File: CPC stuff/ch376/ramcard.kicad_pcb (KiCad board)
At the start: 2 copper layers, 69.1 x 40.4 mm, 17 parts, among them IC1 74LS20, IC2 74LS02, IC3 74LS138, IC4 CH376, P1 CONN_25X2, P2 USB_A, U1 LD1117S33CTR, U2 CONN_SD, Y1 Crystal_Small

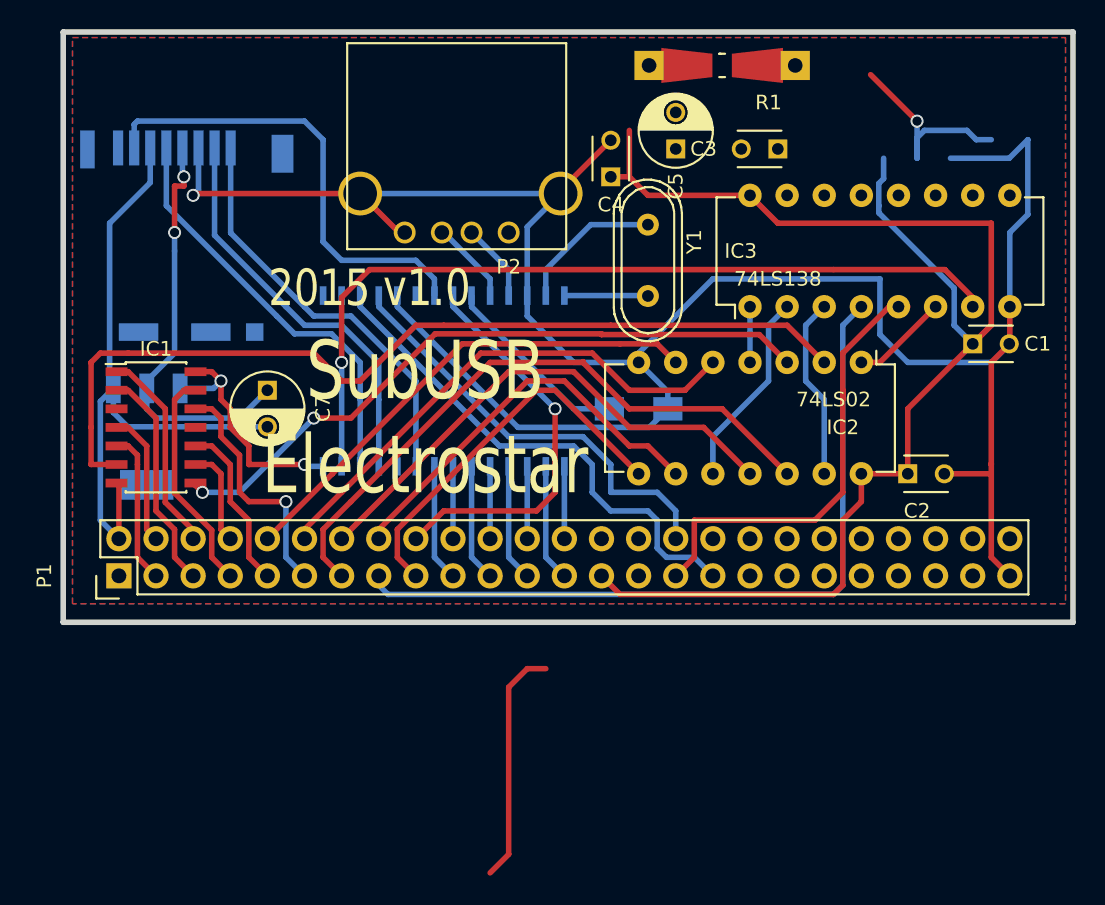
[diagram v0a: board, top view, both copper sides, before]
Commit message: Complete routing of Albireo, including serial port.
git-svn-id: svn://pulkomandy.tk/avrstuff@117 c6672c3c-f6b6-47f9-9001-1fd6b12fecbe
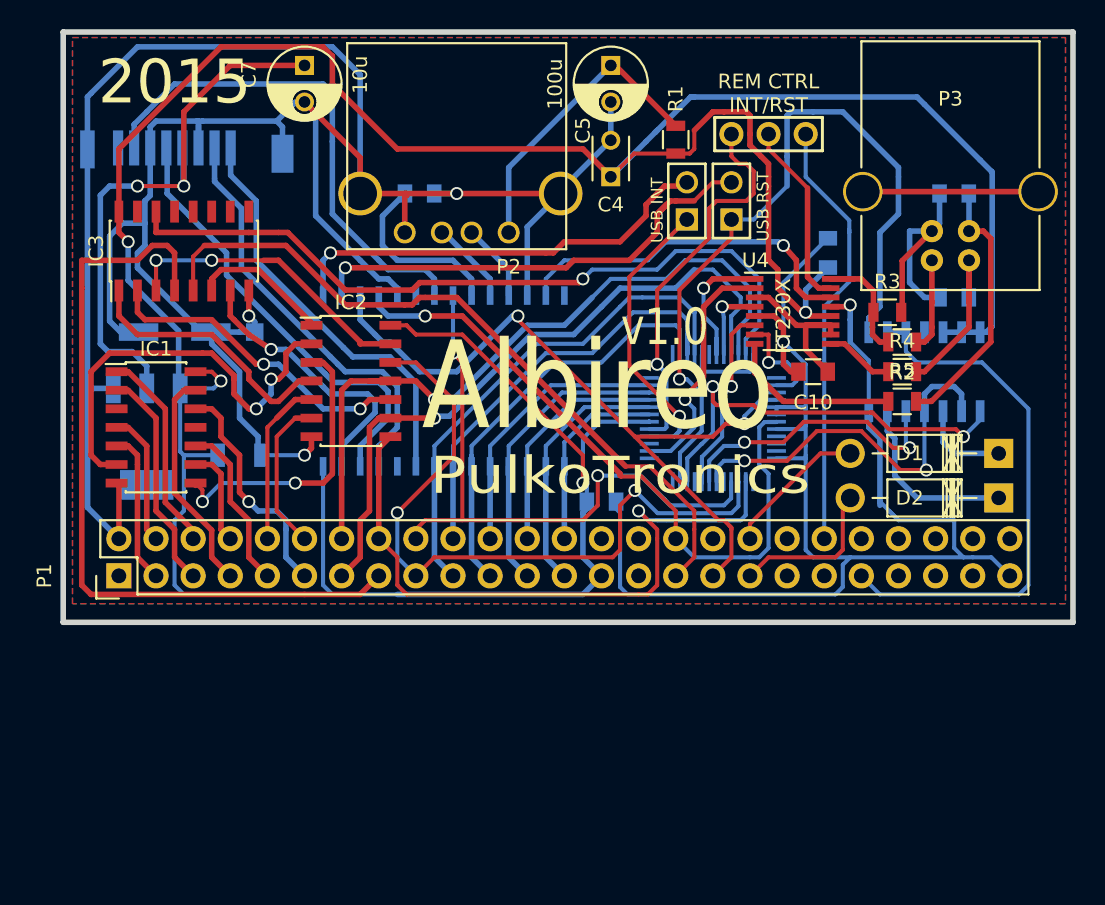
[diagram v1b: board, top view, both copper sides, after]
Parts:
- removed Y1: Crystal_Small, Crystals:Crystal_HC49-U_Vertical
- added C10: C, Capacitors_SMD:C_0805, F.Cu at (69.1, 53.3)
- added C8: 47pF, Capacitors_SMD:C_0805, B.Cu at (78.7, 41.1)
- added C9: 47pF, Capacitors_SMD:C_0805, B.Cu at (78.7, 48.3)
- added D1: D, Diodes_ThroughHole:Diode_DO-41_SOD81_Horizontal_RM10, F.Cu at (81.8, 58.9)
- added D2: D, Diodes_ThroughHole:Diode_DO-41_SOD81_Horizontal_RM10, F.Cu at (81.8, 62.0)
- added JP1: JUMPER3, opendous:SIL-3-Blank, F.Cu at (66.0, 37.1)
- added JP2: USB INT, opendous:SIL-2_Opendous, F.Cu at (60.5, 41.7)
- added JP3: USB RST, opendous:SIL-2_Opendous, F.Cu at (63.5, 41.7)
- added P3: USB_B, Connect:USB_B, F.Cu at (77.2, 45.7)
- added R2: 4k7, Resistors_SMD:R_0805, F.Cu at (75.2, 51.3)
- added R3: 10k, Resistors_SMD:R_0805, F.Cu at (74.2, 49.3)
- added R4: 27, Resistors_SMD:R_0805, F.Cu at (75.2, 53.3)
- added R5: 27, Resistors_SMD:R_0805, F.Cu at (75.2, 55.4)
- added U3: TL16C550C, Housings_QFP:TQFP-48_7x7mm_Pitch0.5mm, B.Cu at (62.2, 56.5)
- added U4: FT230X, Housings_SSOP:SSOP-16_3.9x4.9mm_Pitch0.635mm, F.Cu at (67.7, 49.2)
- added U5: 74LS00, Housings_SOIC:SOIC-14_3.9x8.7mm_Pitch1.27mm, B.Cu at (76.7, 53.3)
- C1, C2: footprint Capacitors_ThroughHole:C_Disc_D3_P2.5 -> Capacitors_SMD:C_0805; moved to B.Cu
- C3: footprint Capacitors_ThroughHole:C_Disc_D3_P2.5 -> Capacitors_SMD:C_1206; moved to B.Cu
- C6: footprint Capacitors_SMD:C_1206_HandSoldering -> Capacitors_SMD:C_0805
- IC2: footprint Housings_DIP:DIP-14_W7.62mm -> Housings_SOIC:SOIC-14_3.9x8.7mm_Pitch1.27mm
- IC3: footprint Housings_DIP:DIP-16_W7.62mm -> Housings_SOIC:SOIC-16_3.9x9.9mm_Pitch1.27mm
- R1: footprint Resistors_Universal:Resistor_SMD+THTuniversal_0805to1206_RM10_HandSoldering -> Resistors_SMD:R_0805
- moved C3 42.4 mm to (29.8, 59.1), turned to 0 degrees
- moved IC3 38.9 mm to (26.0, 45.1)
- moved IC2 34.9 mm to (37.5, 54.0), turned to 0 degrees
- moved C7 22.4 mm to (34.3, 32.4)
- moved C2 21.0 mm to (54.6, 62.2)
- moved C6 21.0 mm to (42.2, 41.1)
- moved C1 11.7 mm to (70.1, 45.2), turned to 90 degrees
- moved C5 7.24 mm to (55.2, 32.4), turned to 270 degrees
- moved R1 5.99 mm to (59.7, 37.5), turned to 270 degrees
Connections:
- IC2 pad 12: /A5 -> /A1
- IC2 pad 5: /A6 -> /A8
- IC2 pad 6: /A8 -> /A6
- IC2 pad 8: /A1 -> /A2
- IC2 pad 9: /A2 -> /A5
- IC3 pad 14: (no net) -> /FEBx
- IC4 pad 1: (no net) -> Net-(IC4-Pad1)
- IC4 pad 13: Net-(IC4-Pad13) -> /12MHz
- IC4 pad 14: Net-(IC4-Pad14) -> (no net)
- IC4 pad 2: (no net) -> Net-(IC4-Pad2)
- P1 pad 35: (no net) -> //INT
- P1 pad 36: (no net) -> //NMI
- P1 pad 40: (no net) -> /BUSRST
- P1 pad 41: (no net) -> //RESET
- U2 pad 9: Net-(U2-Pad9) -> GND
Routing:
- net VCC: track 112.7 -> 274.5 mm, vias 2 -> 4
- net GND: track 203.6 -> 341.5 mm, vias 1 -> 5
- net /PRESET: track 0.00 -> 52.3 mm, vias 0 -> 1
- net /FEBx: track 0.00 -> 51.8 mm, vias 0 -> 1
- net /FE80: track 57.7 -> 19.3 mm
- net //RESET: track 0.00 -> 36.9 mm
- net Net-(IC4-Pad2): track 0.00 -> 32.5 mm, vias 0 -> 1
- net (no net): track 30.3 -> 0.00 mm, vias 1 -> 0
- net Net-(IC4-Pad1): track 0.00 -> 30.0 mm, vias 0 -> 1
- net /BUSRST: track 0.00 -> 29.6 mm
- net //OUT1: track 0.00 -> 28.6 mm, vias 0 -> 2
- net //RI: track 0.00 -> 26.9 mm, vias 0 -> 1
- net /INTRPT: track 0.00 -> 26.8 mm, vias 0 -> 2
- net /D7: track 8.02 -> 34.7 mm
- net Net-(IC1-Pad8): track 46.2 -> 20.0 mm
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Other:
- net class Default: clearance 0.2032 -> 0.2
- rule trace_clearance: 0.2032 -> 0.2
- board text added: "2015"
- board text added: "Albireo"
- board text added: "REM CTRL INT/RST"
- board text added: "v1.0"
- board text removed: "2015 v1.0"
- board text removed: "SubUSB Electrostar"

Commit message: Update following Gerald's coomments  * Use 74LS38 instead of 74LS00 and remove diodes  * Add pull-up for the one pin that doesn't have one (PRESET)  * Optimize layout a bit
git-svn-id: svn://pulkomandy.tk/avrstuff@118 c6672c3c-f6b6-47f9-9001-1fd6b12fecbe
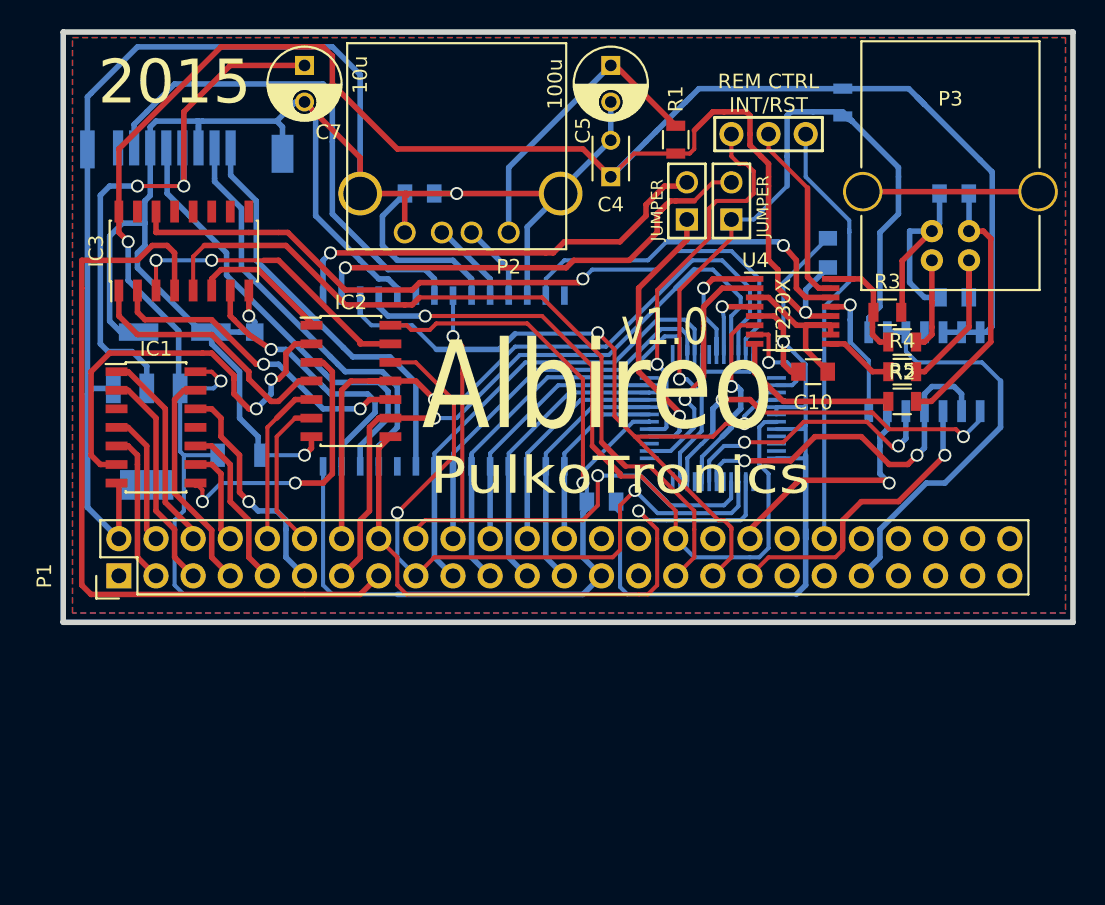
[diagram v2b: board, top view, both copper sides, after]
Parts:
- removed D1, D2: D, Diodes_ThroughHole:Diode_DO-41_SOD81_Horizontal_RM10
- added R6: 4K7, Resistors_SMD:R_0805, B.Cu at (71.1, 34.9)
- JP2: value USB INT -> JUMPER
- JP3: value USB RST -> JUMPER
- U5: value 74LS00 -> 74LS38
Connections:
- U5 pad 3: Net-(D1-Pad1) -> //INT
- U5 pad 6: Net-(D2-Pad1) -> //NMI
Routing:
- net GND: track 341.5 -> 314.1 mm
- net Net-(D2-Pad1): track 12.4 -> 0.00 mm
- net //INT: track 10.9 -> 21.0 mm, vias 0 -> 1
- net //RESET: track 36.9 -> 27.9 mm
- net //NMI: track 9.87 -> 17.3 mm, vias 0 -> 1
- net Net-(D1-Pad1): track 6.25 -> 0.00 mm
- net //IORQ: track 49.9 -> 53.3 mm
- net VCC: track 274.5 -> 277.8 mm
- net /D6: track 30.7 -> 27.5 mm
- net //RD: track 47.4 -> 50.6 mm
- net /D7: track 34.7 -> 32.5 mm
- net //OUT1: track 28.6 -> 26.5 mm
- net /INTRPT: track 26.8 -> 25.1 mm
- net /PRESET: track 52.3 -> 53.7 mm
- net /D5: track 30.6 -> 29.3 mm
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
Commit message: A lot of tweaking and small fixes.
git-svn-id: svn://pulkomandy.tk/avrstuff@119 c6672c3c-f6b6-47f9-9001-1fd6b12fecbe
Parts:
- removed JP1: JUMPER3, opendous:SIL-3-Blank
- removed JP2, JP3: JUMPER, opendous:SIL-2_Opendous
- added R7: 4k7, Resistors_SMD:R_0805, F.Cu at (72.9, 48.3)
- added S1: SW_DIP_x4, Buttons_Switches_ThroughHole:SW_DIP_x4_Slide, F.Cu at (67.3, 41.3)
- C3: footprint Capacitors_SMD:C_1206 -> Capacitors_SMD:C_0805
- R2, R3: moved to B.Cu
- U4: value FT230X -> FT231X; footprint Housings_SSOP:SSOP-16_3.9x4.9mm_Pitch0.635mm -> ch376:SSOP-24_3.9x8.7mm_Pitch0.635mm
- moved R6 13.1 mm to (74.3, 47.6), turned to 180 degrees
- moved R2 11.4 mm to (69.8, 41.3), turned to 270 degrees
- moved P3 9.65 mm to (72.0, 37.6), turned to 0 degrees
- moved C9 8.08 mm to (73.0, 42.5), turned to 0 degrees
- moved R1 7.24 mm to (55.2, 43.2), turned to 90 degrees
- moved R5 7.22 mm to (76.5, 48.3), turned to 90 degrees
- moved R4 5.11 mm to (74.7, 48.3), turned to 90 degrees
- moved R3 4.68 mm to (73.2, 44.7)
- moved C8 3.42 mm to (76.2, 38.9), turned to 90 degrees
- moved C1 3.23 mm to (67.8, 47.5), turned to 180 degrees
- moved C10 2.22 mm to (68.2, 55.4)
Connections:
- IC4 pad 1: Net-(IC4-Pad1) -> /INT
- IC4 pad 2: Net-(IC4-Pad2) -> /RSTI
- P1 pad 46: (no net) -> /CURSOR
- U3 pad 39: (no net) -> //DSR
- U3 pad 41: //RI -> /CURSOR
- U4 pad 1: /RX -> /GPO2
- U4 pad 10: Net-(C10-Pad1) -> /24MHz
- U4 pad 11: Net-(C10-Pad1) -> Net-(R5-Pad1)
- U4 pad 12: VCC -> Net-(R4-Pad1)
- U4 pad 13: GND -> Net-(C10-Pad1)
- U4 pad 14: /12MHz -> VCC
- U4 pad 15: /GPO2 -> VCC
- U4 pad 16: /VBUS_Sense -> GND
- U4 pad 5: GND -> (no net)
- U4 pad 6: //RTS -> GND
- U4 pad 7: /24MHz -> (no net)
- U4 pad 8: Net-(R5-Pad1) -> (no net)
- U4 pad 9: Net-(R4-Pad1) -> //RTS
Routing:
- net GND: track 314.1 -> 437.4 mm, vias 5 -> 6
- net /INT: track 0.00 -> 49.1 mm, vias 0 -> 2
- net /CURSOR: track 0.00 -> 37.4 mm, vias 0 -> 1
- net /RSTI: track 0.00 -> 35.2 mm, vias 0 -> 2
- net VCC: track 277.8 -> 244.7 mm
- net Net-(IC4-Pad2): track 32.5 -> 0.00 mm, vias 1 -> 0
- net Net-(IC4-Pad1): track 30.0 -> 0.00 mm, vias 1 -> 0
- net //RI: track 26.9 -> 0.00 mm, vias 1 -> 0
- net //DSR: track 0.00 -> 23.1 mm, vias 0 -> 1
- net Net-(P3-Pad5): track 12.0 -> 0.00 mm
- net +3V3: track 51.6 -> 40.1 mm
- net /A1: track 48.4 -> 59.8 mm
- net /GPO2: track 12.8 -> 23.6 mm
- net /A8: track 16.8 -> 27.1 mm
- net //DCD: track 19.7 -> 28.6 mm
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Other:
- board text added: "1 CH376 INT enable 2 CH376 Reset enable 3 Rem.ctrl resets CPC 4 Rem.ctrl triggers interrupt"
- board text added: "uSD"
- board text added: "v0.9"
- board text removed: "REM CTRL INT/RST"
- board text removed: "v1.0"

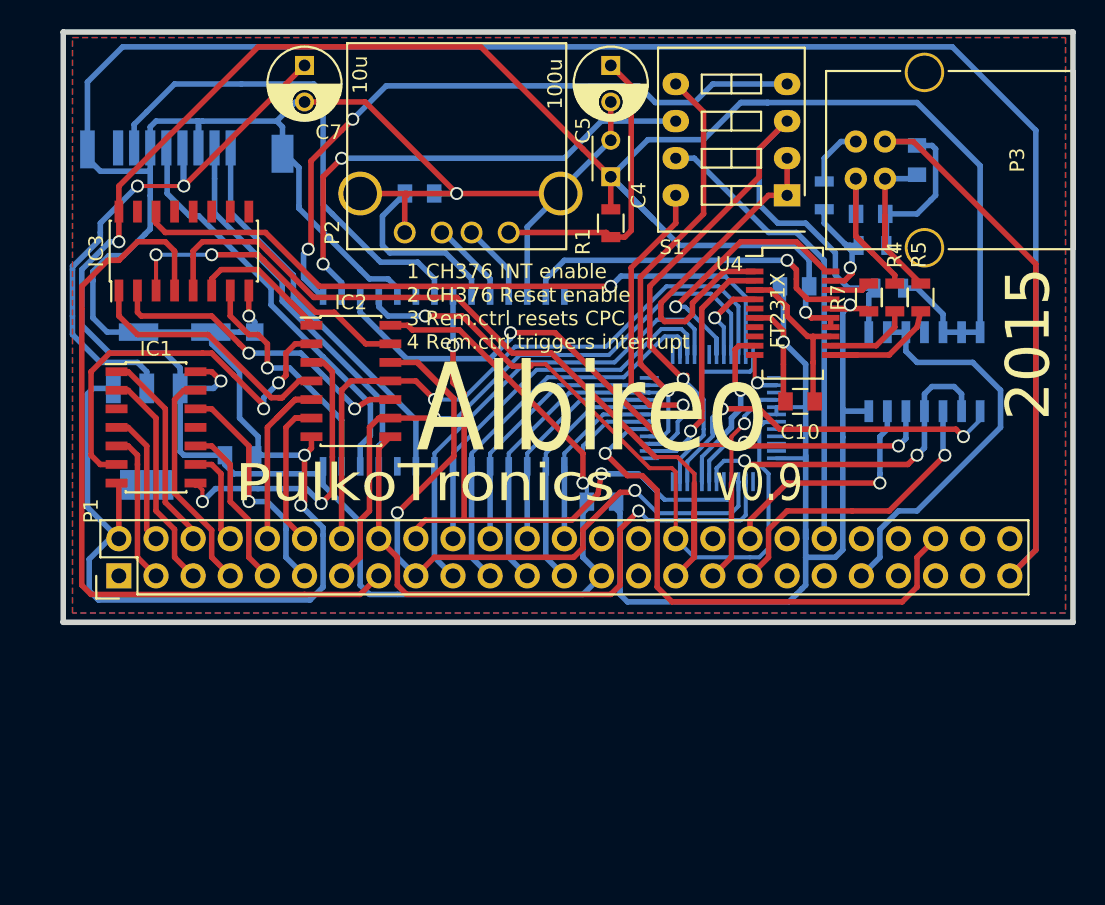
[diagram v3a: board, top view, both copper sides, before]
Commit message: Fixes after testing of prototype batch.
git-svn-id: svn://pulkomandy.tk/avrstuff@120 c6672c3c-f6b6-47f9-9001-1fd6b12fecbe
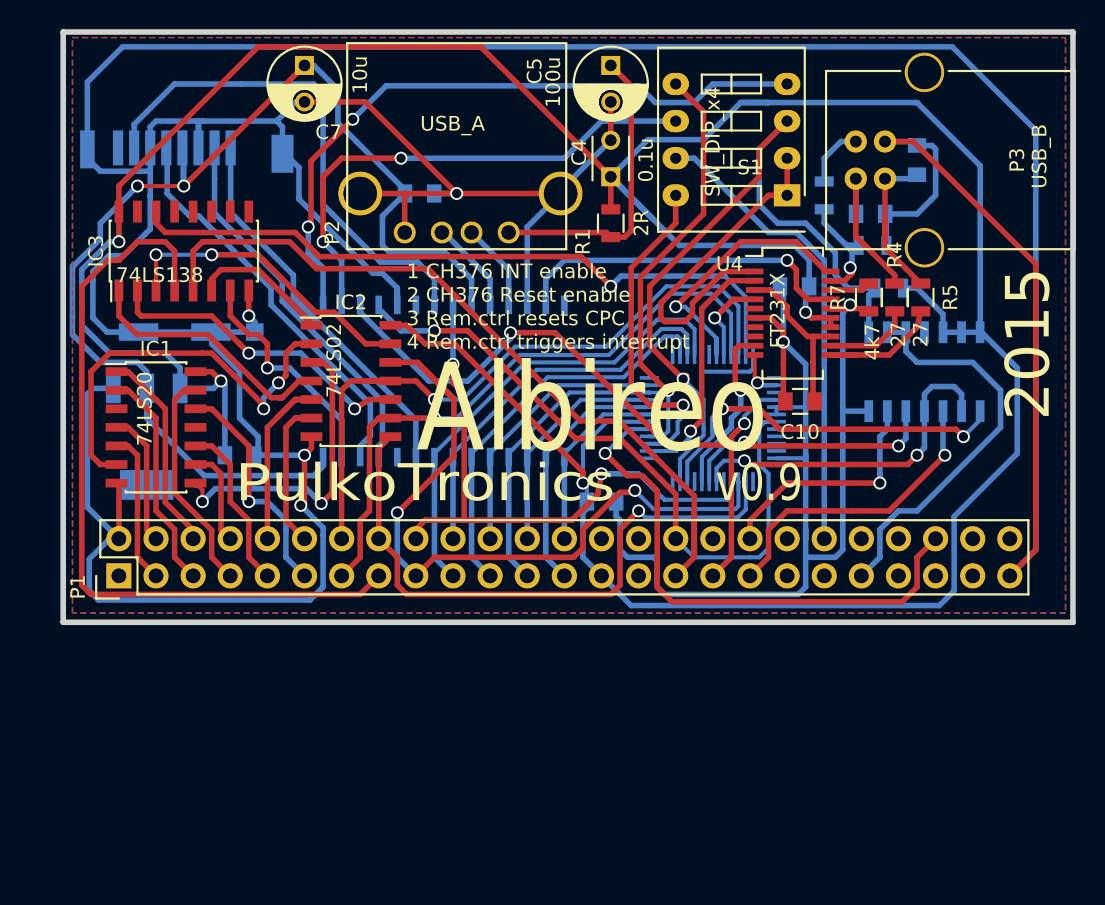
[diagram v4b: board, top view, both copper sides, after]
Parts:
- C1: value C -> 1uF
- C10: value C -> 100nF
- C6: value 0.01u -> 10nF
- IC4: footprint SMD_Packages:SOJ-28-W -> ch376:CH376_SOJ28
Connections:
- C6 pad 1: Net-(C6-Pad1) -> +3V3
- IC4 pad 28: VCC -> +3V3
- IC4 pad 9: Net-(C6-Pad1) -> +3V3
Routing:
- net +3V3: track 40.1 -> 80.5 mm
- net VCC: track 244.7 -> 272.6 mm
- net Net-(C6-Pad1): track 12.4 -> 0.00 mm
- net GND: track 437.4 -> 446.6 mm
- net /A2: track 53.8 -> 47.7 mm
- net //RD: track 49.1 -> 46.3 mm
- net //WR: track 50.0 -> 52.5 mm
- net //IORQ: track 61.9 -> 61.0 mm
- net /A0: track 44.9 -> 44.3 mm
- net /FE80: track 16.5 -> 15.8 mm
- net /SD_CLK: track 28.2 -> 27.6 mm
- net //SD_CS: track 27.0 -> 26.4 mm
- net /SD_DI: track 26.7 -> 26.0 mm
